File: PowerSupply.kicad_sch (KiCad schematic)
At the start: 6 parts, among them U6 TPS62177DQC

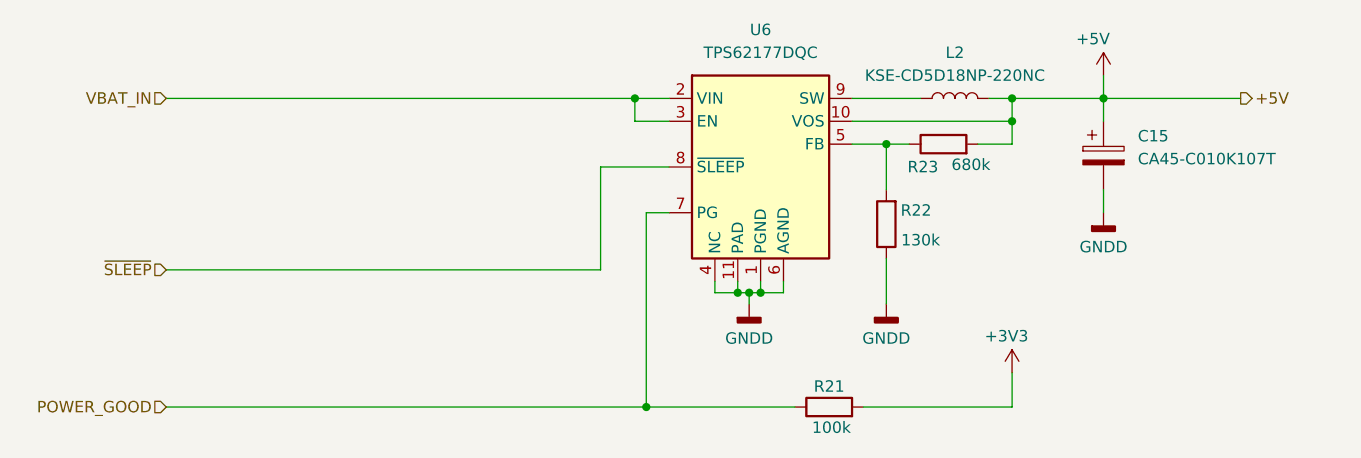
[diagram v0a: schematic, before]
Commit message: Move to SIM800C-DS and two SIM
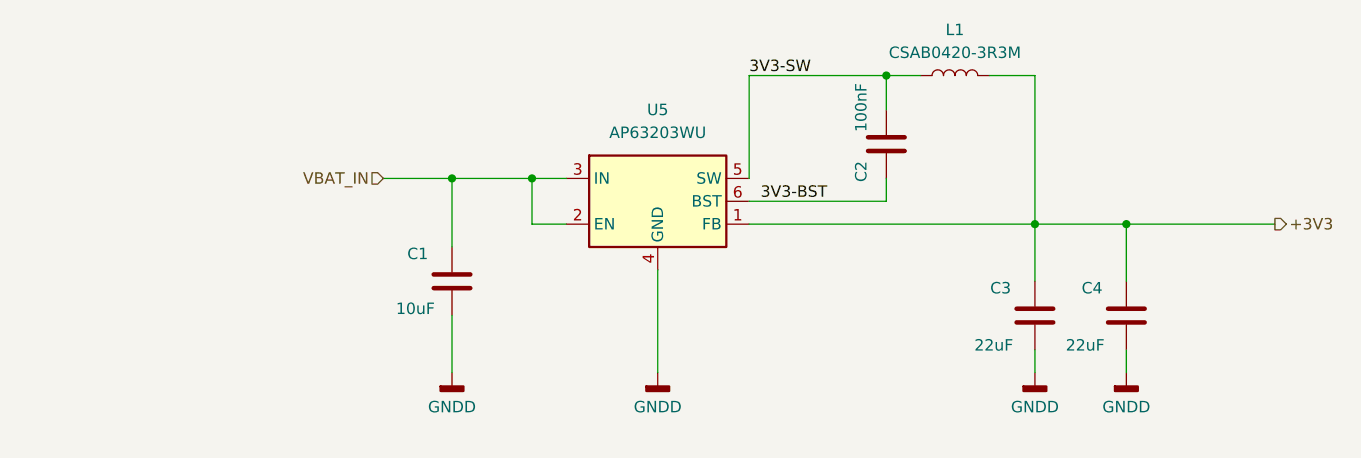
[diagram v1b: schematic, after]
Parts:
- removed C15: CA45-C010K107T, Capacitor_Tantalum_SMD:CP_EIA-6032-28_Kemet-C_Pad2.25x2.35mm_HandSolder, symbol Device:C_Polarized
- removed L2: KSE-CD5D18NP-220NC, Inductor_SMD:L_Cenker_CKCS6028, symbol Device:L
- removed R21: 100k, Resistor_SMD:R_0805_2012Metric_Pad1.20x1.40mm_HandSolder, symbol Device:R
- removed R22: 130k, Resistor_SMD:R_0805_2012Metric_Pad1.20x1.40mm_HandSolder, symbol Device:R
- removed R23: 680k, Resistor_SMD:R_0805_2012Metric_Pad1.20x1.40mm_HandSolder, symbol Device:R
- removed U6: TPS62177DQC, Package_SON:WSON-10-1EP_2x3mm_P0.5mm_EP0.84x2.4mm_ThermalVias, symbol Regulator_Switching:TPS62177DQC
- added C1: 10uF, Capacitor_SMD:C_0805_2012Metric_Pad1.18x1.45mm_HandSolder, symbol Device:C
- added C2: 100nF, Capacitor_SMD:C_0805_2012Metric_Pad1.18x1.45mm_HandSolder, symbol Device:C
- added C3, C4: 22uF, Capacitor_SMD:C_0805_2012Metric_Pad1.18x1.45mm_HandSolder, symbol Device:C
- added L1: CSAB0420-3R3M, footprints:CSAB0420-4.4x4.4mm, symbol Device:L
- added U5: AP63203WU, Package_TO_SOT_SMD:TSOT-23-6, symbol Regulator_Switching:AP63203WU
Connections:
- net +3V3: now also C3.2, C4.2, L1.2, U5.1 (FB)
- net GNDD: now also C1.1, C3.1, C4.1, U5.4 (GND)
- net VBAT_IN: now also C1.2, U5.2 (EN), U5.3 (IN)
- new net 3V3-BST: C2.1, U5.6 (BST)
- new net 3V3-SW: C2.2, L1.1, U5.5 (SW)
